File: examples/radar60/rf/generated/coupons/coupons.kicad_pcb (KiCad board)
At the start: 6 copper layers, 60 x 25 mm, 82 parts, among them J60A SMA-J-P-H-ST-EM1, J60B SMA-J-P-H-ST-EM1, J61A SMA-J-P-H-ST-EM1, J61B SMA-J-P-H-ST-EM1, J6RA SMA-J-P-H-ST-EM1, J6RB SMA-J-P-H-ST-EM1

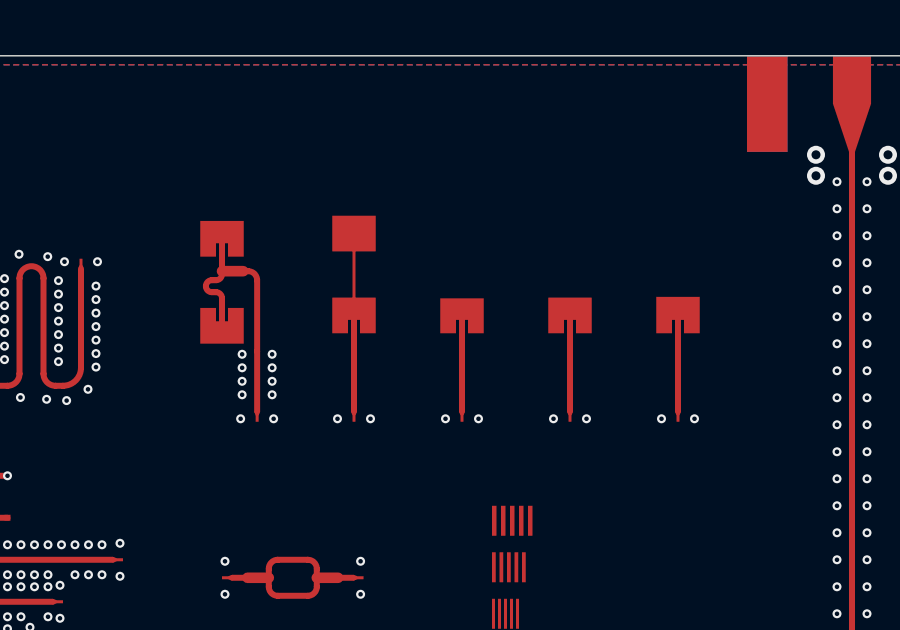
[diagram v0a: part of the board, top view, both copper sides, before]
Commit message: radar60 rf: openEMS first validation and full-wave patch calibration
First EM validation of the conventional column (two patches on L2
windows, corporate divider, gap input) in openEMS v0.37.0-rc3 on the
Mac (Docker, 4 threads, 1.25 M cells, about 14 min per run; no GCP):

- as drawn from closed form the patch resonates at 60.0 GHz, not
  62.05 (-3.3 %), and the column never reaches RL 10 dB (best 9.2 dB at
  60.2 GHz); realized broadside gain 0.0 dBi at 62.05 GHz (7.4 at 60.3)
  against 9.2 dBi predicted;
- a via ring round each window (L2-L3 stitching) does not help;
- a three-point single-patch sweep (L x0.967, inset 0.30/0.38/0.45,
  picked by |S11| at 62.05 GHz) matches the patch (RL >= 10 dB
  60.90-62.80 GHz, -26.9 dB at 61.9 GHz); the column with it reaches
  6.3 / 7.7 / 6.9 dBi realized gain at 60.3 / 62.05 / 63.8 GHz,
  directivity 9.4 dBi, radiation efficiency 70-78 %, but its input is
  still mismatched in band (RL 5.9 / 9.1 / 11.4 dB), which C1 sizes.

The generator now draws L = closed-form L x 0.967 with inset 0.30 mm
(declared parameters citing results/openems/patch-c-i30); the D12
variants bracket the calibrated length. column_sim.py gains a matched
feed (Feed_R 50), a single-patch diagnostic and an optional window via
ring; summarize.py tabulates runs against the closed-form predictions.
All four boards regenerated; KiCad 10.0.6 DRC still reports no
violations and no unconnected items.

Co-Authored-By: Claude Opus 5.5 <noreply@anthropic.com>
Claude-Session: https://claude.ai/code/session_014FiHUDEn5jCP4V8pPjQkPy
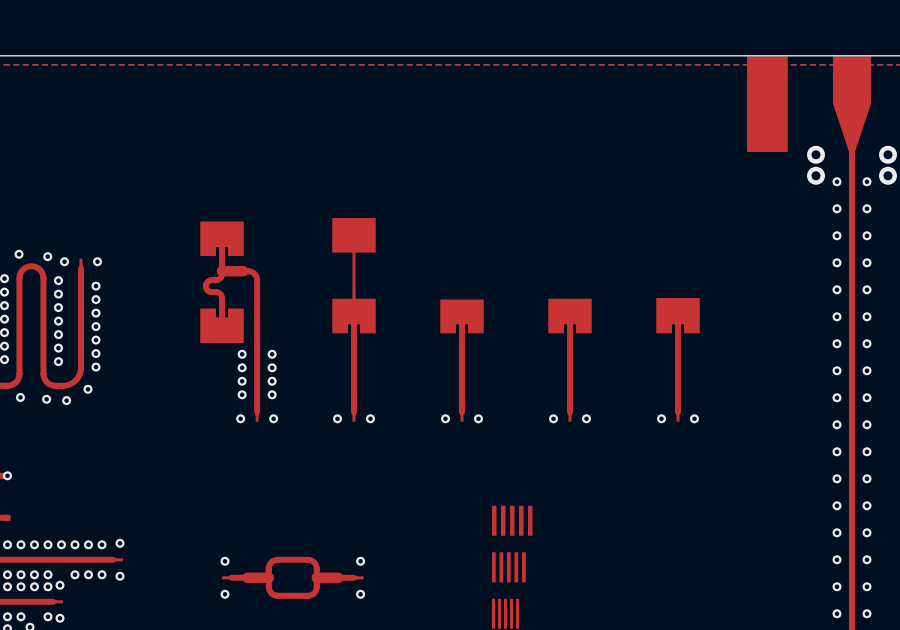
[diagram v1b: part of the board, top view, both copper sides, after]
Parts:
- moved CP54 0.06 mm to (113.9, 81.0)

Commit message: radar60 rf: review fixes (via rules, In2 clip, L2-L3 stitching, placeholder status)
- Fence and isolation vias 0.15/0.32 (the profile's 3 mil ring) with no two vias closer than
  0.43 mm (11 mil hole to hole); the coupon strip likewise. Integration DRC found 288 via and
  2 hole-to-hole violations with the old 0.30 pad and 0.40 spacing.
- In2.Cu GND only where the macro needs its L3 reference: the RF region outside the package,
  the under-package ground of rows 1-3 and A-C, and each land's L2 cut-out plus 0.3 mm. Under
  the rest of the package In2 is the board's escape layer. The outlines go into each record
  (board_frame.in2_gnd_polygons) for the fanout. The macro region now starts at the east pour
  (U1 y -1.3), as the board's RF region does.
- L2-L3 stitching: 208 GND through vias every 0.6 mm (lambda_d/4 in RO4450F at 62 GHz is
  0.64 mm) round each bank (1.4 mm from the patches) and inside the In2 GND boundary. Not
  simulated yet: the C2 bank solve has to report it.
- Every record carries status "placeholder": the column fails ANT-02 RL at P1 (col-c), the
  calibration came from one patch, C1 and C2 come before the macro is frozen.

rfm1-m/-n/-p and the coupon strip: KiCad DRC clean, no unconnected items.

Co-Authored-By: Claude Opus 5.5 <noreply@anthropic.com>
Claude-Session: https://claude.ai/code/session_014FiHUDEn5jCP4V8pPjQkPy
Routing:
- net GND: vias 239 -> 227

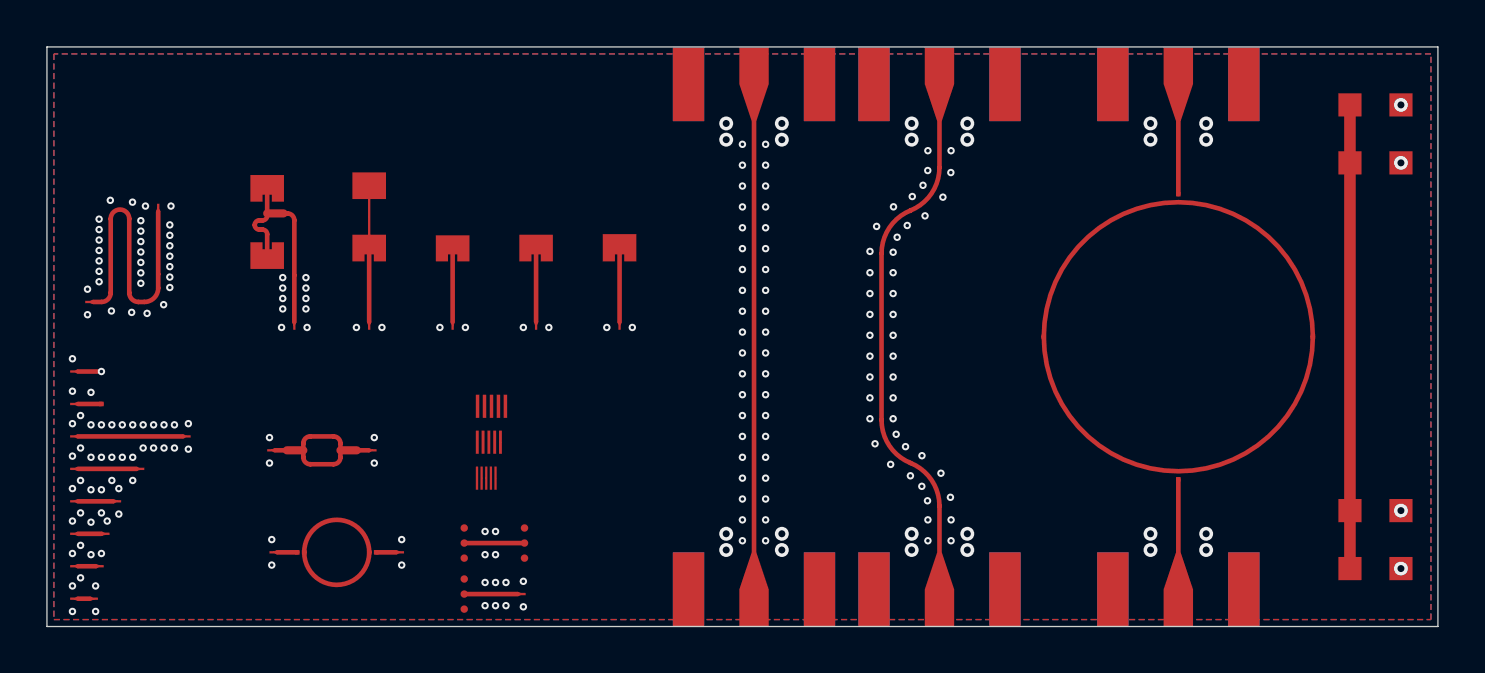
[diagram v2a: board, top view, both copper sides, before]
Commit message: radar60 rf: regenerate rfm1-m/n/p and the coupon strip; README
Generator checks pass for all three D12 variants (outside-cut-out hash
identical); kicad-cli pcb drc --refill-zones --severity-all: no
violations, no unconnected items on rfm1-m, -n, -p and the coupon strip.

board_frame (U1 at 26, 28) [D]: RX phase centres y 39.988 (x unchanged),
TX x 38.718 / 41.060 / 43.402 at y 38.100; cut-outs RX 16.599-32.205 x
36.688-43.024, TX 34.205-47.469 x 34.800-41.136; region x 12.599-51.469,
y 26.7-47.024; R4 guard x 7.599-56.469; board height >= 47.349; nearest
active RX-TX phase centres 11.19 mm; loads RL1-RL4.

README: new geometry, the uniformity rules, the checks, the floorplan, the
coupons, the audit and test commands; the integration (kicad_ops) still has
to take the dummy footprints and loads.

Co-Authored-By: Claude Opus 5.5 <noreply@anthropic.com>
Claude-Session: https://claude.ai/code/session_014FiHUDEn5jCP4V8pPjQkPy
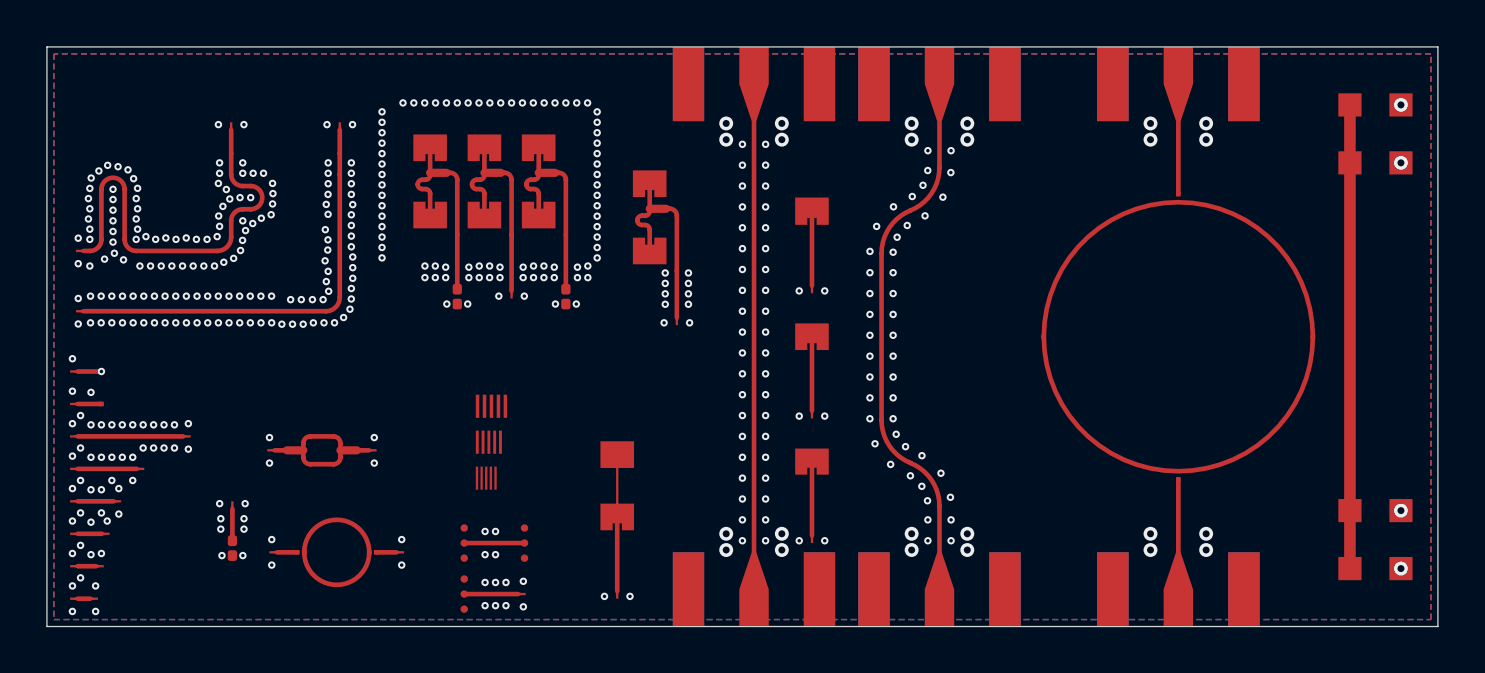
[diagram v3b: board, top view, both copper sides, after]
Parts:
- removed the CP48 at (101.8, 86.0)
- removed the CP49 at (104.8, 81.9)
- added CP15: cpz, radar60:CP_PAD, F.Cu at (108.0, 94.8)
- added CP53: cpt/TX1/a, radar60:CP_PAD, F.Cu at (101.4, 83.8)
- added CP54: cpt/TX1/b, radar60:CP_PAD, F.Cu at (107.9, 78.4)
- added CP55: cpt/TX3/a, radar60:CP_PAD, F.Cu at (101.4, 86.4)
- added CP56: cpt/TX3/b, radar60:CP_PAD, F.Cu at (112.6, 78.4)
- added CP63: cpa/cell/2/1, radar60:CP_PAD, F.Cu at (121.2, 79.3)
- added CP67: cpa/pM25, radar60:CP_PAD, F.Cu at (133.0, 92.9)
- added CP68: cpa/pM25, radar60:CP_PAD, F.Cu at (133.0, 96.2)
- added CP69: cpa/pNOM, radar60:CP_PAD, F.Cu at (133.0, 87.5)
- added CP70: cpa/pNOM, radar60:CP_PAD, F.Cu at (133.0, 90.8)
- added CP71: cpa/pP25, radar60:CP_PAD, F.Cu at (133.0, 82.1)
- added CP72: cpa/pP25, radar60:CP_PAD, F.Cu at (133.0, 85.4)
- added RLA0: 50R 0201 thin film, radar60:R_0201_0603Metric_LOAD, F.Cu at (117.7, 85.8)
- added RLA2: 50R 0201 thin film, radar60:R_0201_0603Metric_LOAD, F.Cu at (122.4, 85.8)
- added RLZ1: 50R 0201 thin film, radar60:R_0201_0603Metric_LOAD, F.Cu at (108.0, 96.6)
- CP57: value cpa/pM25 -> cpa/cell/0/0
- CP58: value cpa/pM25 -> cpa/cell/0/1
- CP59: value cpa/pNOM -> cpa/cell/1/0
- CP60: value cpa/pNOM -> cpa/cell/1/1
- CP61: value cpa/pP25 -> cpa/cell
- CP62: value cpa/pP25 -> cpa/cell/2/0
- moved CP64 16.5 mm to (126.0, 83.8)
- moved CP65 16.5 mm to (126.0, 80.9)
- moved CP66 16.5 mm to (127.2, 86.8)
- moved CP50 15.8 mm to (124.6, 92.6)
- moved CP51 15.8 mm to (124.6, 93.9)
- moved CP49 15.8 mm to (124.6, 95.3)
- moved CP52 15.8 mm to (124.6, 98.6)
- moved CP60 7.99 mm to (118.9, 79.3)
- moved CP58 7.74 mm to (116.5, 79.3)
- moved CP62 5.91 mm to (121.2, 82.2)
- moved CP61 5.07 mm to (120.0, 85.7)
- moved CP59 2.65 mm to (118.9, 82.2)
- moved CP57 1.73 mm to (116.5, 82.2)
- renumbered CP15 to CP16, CP16 to CP17, CP17 to CP18, CP18 to CP19, CP19 to CP20, CP20 to CP21, CP21 to CP22, CP22 to CP23, CP23 to CP24, CP24 to CP25, CP25 to CP26, CP26 to CP27, CP27 to CP28, CP28 to CP29, CP29 to CP30, CP30 to CP31, CP31 to CP32, CP32 to CP33, CP33 to CP34, CP34 to CP35, CP35 to CP36, CP36 to CP37, CP37 to CP38, CP38 to CP39, CP39 to CP40, CP40 to CP41, CP41 to CP42, CP42 to CP43, CP43 to CP44, CP44 to CP45, CP45 to CP46, CP46 to CP47, CP47 to CP48, CP53 to CP49, CP54 to CP50, CP55 to CP51, CP56 to CP52, CP50 to CP64, CP51 to CP65, CP52 to CP66, CP63 to CP73, CP64 to CP74, CP65 to CP75, CP66 to CP76, CP67 to CP77, CP68 to CP78, CP69 to CP79, CP70 to CP80, CP71 to CP81, CP72 to CP82, CP73 to CP83, CP74 to CP84
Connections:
- net CPA_PM25 renamed CPA_D0
- CP59 pad 1: CPA_PNOM -> CPA_CELL
- CP60 pad 1: CPA_PNOM -> CPA_CELL
- CP61 pad 1: CPA_PP25 -> CPA_CELL
- CP62 pad 1: CPA_PP25 -> CPA_D2
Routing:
- net CPT_TX3: track 0.00 -> 18.5 mm
- net CPA_CELL: track 0.00 -> 9.15 mm
- net CPA_D2: track 0.00 -> 9.10 mm
- net CPA_D0: track 2.90 -> 9.10 mm
- net CPT_TX1: track 13.5 -> 18.2 mm
- net CPA_PM25: track 0.00 -> 2.90 mm
- net CPZ_LOAD: track 0.00 -> 1.35 mm
- net GND: vias 227 -> 437

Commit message: radar60 rf: review fixes of the RF-uniformity layout (loads, G2, G7, audit, coupons)
- Dummy loads: one load cell. Fill vias had landed in three of the four
  0201 GND lands (and differently in each). Each load now has its own five
  vias (pad edges >= 0.14 mm from either land), no other via in its via
  zone, a solder-mask island so the GND land is mask-defined and its vias
  tented, and references RT1-RT4 (RL1/RL2 are the board's radome lands).
  The lands are copper, not pour, for the stitch-reach check. New G7: the
  load cells are identical and no via comes within 0.10 mm of a land.
- G2: the congruence window is symmetric (+-(2d - W/2 - margin)) against
  an interior column. The one declared difference (the absent
  second-neighbour input at an open bank end, RX1 and TX3: 0.95 mm2 of
  copper, 2 vias) is masked and reported.
- Board audit: A1 measures a contact along the cut-out boundary (the x
  extent read TX1's 0.96 mm side contact as 0.05). A2 also compares In1
  and In2 and uses G2's window. New A6: vias at SMD lands. pcbnew is
  imported lazily, so the audits run in the unit tests.
- Regression fixture: the pre-fix rfm1-n (ab57757), KiCad-filled. A1-A4
  must fail on it (RX2/RX3 0.87 mm, TX2 1.48 mm, TX1 two contacts).
- Coupons: CP-T2 (TX2) joins CP-T/CP-T3; without it TX2's corridor was a
  1.3 mm GND channel with a TE10 cut-off near 63 GHz. CP-A gets the
  guard-band rows. The 60 GHz part of the strip is stitched (edge rows,
  0.6 mm grid, fill) and checked like G3. The loads sit under mask islands.
- Regenerated rfm1-m/n/p and the strip. KiCad DRC is clean on all four,
  and A1-A6 pass on the filled m, n and p.

Co-Authored-By: Claude Opus 5.5 <noreply@anthropic.com>
Claude-Session: https://claude.ai/code/session_014FiHUDEn5jCP4V8pPjQkPy
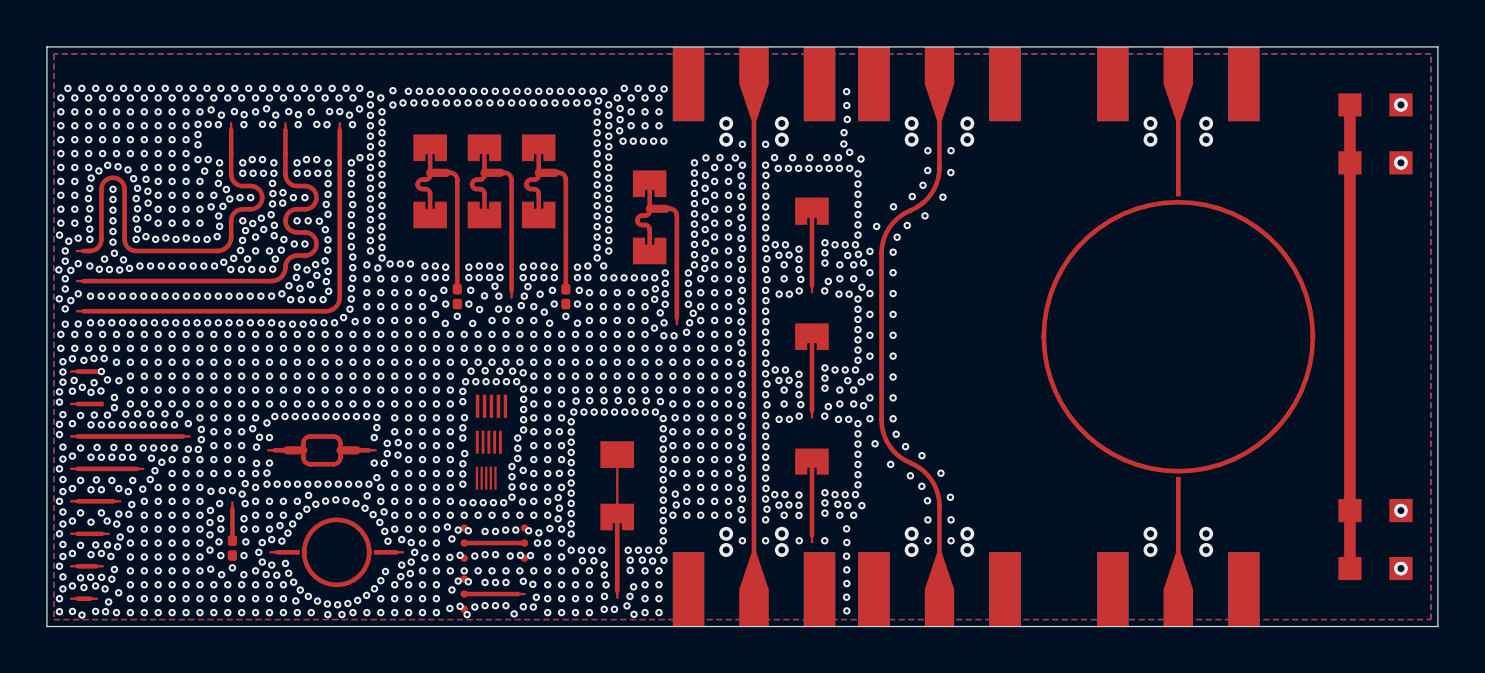
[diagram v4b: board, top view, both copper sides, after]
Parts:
- removed the CP67 at (133.0, 92.9)
- removed the CP68 at (133.0, 96.2)
- removed RLA0, RLA2, RLZ1: 50R 0201 thin film, radar60:R_0201_0603Metric_LOAD
- added CP55: cpt/TX2/a, radar60:CP_PAD, F.Cu at (101.4, 85.1)
- added CP56: cpt/TX2/b, radar60:CP_PAD, F.Cu at (110.3, 78.4)
- added CP73: cpa/pP25, radar60:CP_PAD, F.Cu at (133.0, 82.1)
- added CP74: cpa/pP25, radar60:CP_PAD, F.Cu at (133.0, 85.4)
- added RTA0: 50R 0201 thin film, radar60:R_0201_0603Metric_LOAD, F.Cu at (117.7, 85.8)
- added RTA2: 50R 0201 thin film, radar60:R_0201_0603Metric_LOAD, F.Cu at (122.4, 85.8)
- added RTZ1: 50R 0201 thin film, radar60:R_0201_0603Metric_LOAD, F.Cu at (108.0, 96.6)
- CP69, CP70: value cpa/pNOM -> cpa/pM25
- CP71, CP72: value cpa/pP25 -> cpa/pNOM
- moved CP71 5.41 mm to (133.0, 87.5)
- moved CP72 5.40 mm to (133.0, 90.8)
- moved CP69 5.39 mm to (133.0, 92.9)
- moved CP70 5.38 mm to (133.0, 96.2)
- renumbered CP55 to CP57, CP56 to CP58, CP57 to CP59, CP58 to CP60, CP59 to CP61, CP60 to CP62, CP61 to CP63, CP62 to CP64, CP63 to CP65, CP64 to CP66, CP65 to CP67, CP66 to CP68, CP73 to CP75, CP74 to CP76, CP75 to CP77, CP76 to CP78, CP77 to CP79, CP78 to CP80, CP79 to CP81, CP80 to CP82, CP81 to CP83, CP82 to CP84, CP83 to CP85, CP84 to CP86
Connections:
- CP69 pad 1: CPA_PNOM -> CPA_PM25
- CP70 pad 1: CPA_PNOM -> CPA_PM25
- CP71 pad 1: CPA_PP25 -> CPA_PNOM
- CP72 pad 1: CPA_PP25 -> CPA_PNOM
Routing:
- net CPT_TX2: track 0.00 -> 18.2 mm
- net GND: vias 437 -> 1843
